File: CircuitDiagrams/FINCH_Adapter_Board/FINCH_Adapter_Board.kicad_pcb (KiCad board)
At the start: 2 copper layers, 195 x 101.7 mm, 59 parts, among them J1 CONN_02X20, J2 CONN_02X25, J3 CONN_02X10, J4 CONN_01X07, J5 CONN_01X10, SW1 DIPS_04, U1 7417, U10 74LS163, U11 74LS163, U12 74LS163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

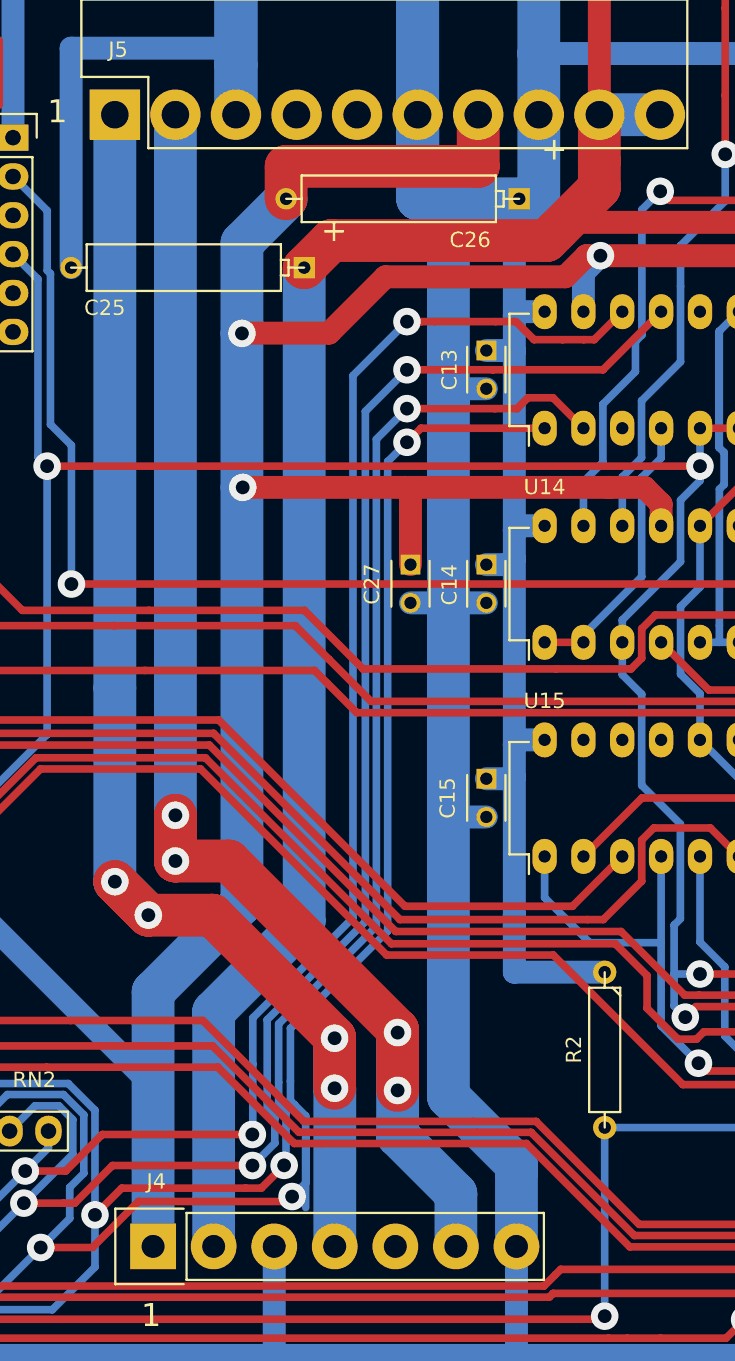
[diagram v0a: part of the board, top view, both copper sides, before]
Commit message: change 24V power supply a bit
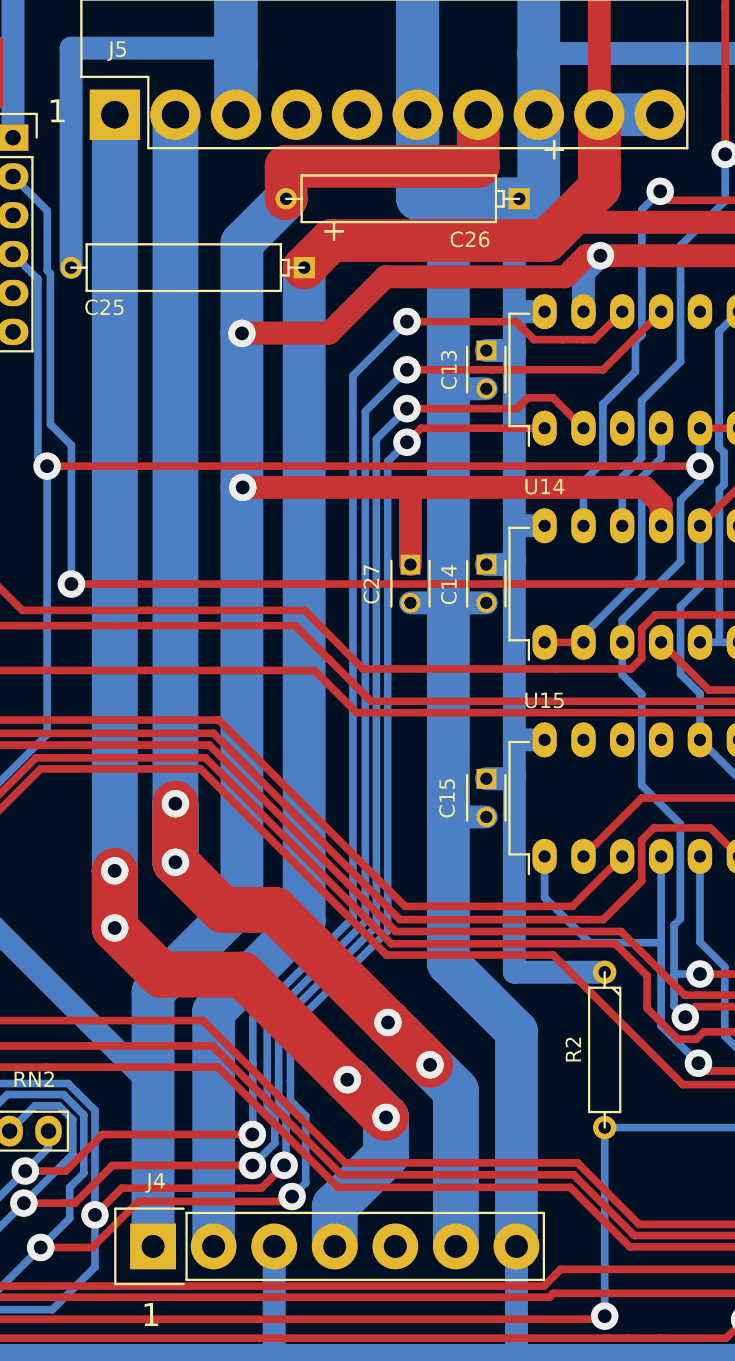
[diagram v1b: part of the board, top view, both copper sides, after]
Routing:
- net Net-(J4-Pad4): track 95.0 -> 100.7 mm
- net /FINCH_Adapter_Board_02/DRV_DATA_SERVO_READ_CLK_-: track 121.2 -> 116.6 mm
- net GND: track 1452.1 -> 1454.2 mm
- net Net-(J4-Pad6): track 93.6 -> 95.2 mm

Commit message: fix some stuff
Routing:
- net -5V: track 313.3 -> 300.3 mm
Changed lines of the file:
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@@
   (segment (start 53.57 135.7) (end 53.57 129.2) (width 1.5) (layer B.Cu) (net 2))
   (segment (start 146.44 135.7) (end 207.4 135.7) (width 1.5) (layer B.Cu) (net 2))
+  (segment (start 97.4 111.93) (end 91.22 111.93) (width 1.5) (layer B.Cu) (net 3))
+  (segment (start 91.22 111.93) (end 86.28 106.99) (width 1.5) (layer B.Cu) (net 3))
   (segment (start 85.61 106.99) (end 86.28 106.99) (width 1.5) (layer B.Cu) (net 3))
-  (segment (start 97.4 118.11) (end 97.4 128.57) (width 1.5) (layer B.Cu) (net 3))
-  (segment (start 86.28 106.99) (end 97.4 118.11) (width 1.5) (layer B.Cu) (net 3))
+  (segment (start 83.05 106.99) (end 85.61 106.99) (width 1.5) (layer B.Cu) (net 3))
   (segment (start 191.01 69.99) (end 195.78 69.99) (width 1.5) (layer F.Cu) (net 3))
   (segment (start 209.08 69.99) (end 210.64 69.99) (width 1.5) (layer F.Cu) (net 3))
@@
   (segment (start 71.62 108.09) (end 73.12 109.59) (width 1.5) (layer B.Cu) (net 3))
   (segment (start 82.47 107.57) (end 83.05 106.99) (width 1.5) (layer B.Cu) (net 3))
-  (segment (start 83.05 106.99) (end 85.61 106.99) (width 1.5) (layer B.Cu) (net 3))
   (segment (start 106.1 60.07) (end 103.21 62.96) (width 2.8) (layer B.Cu) (net 3))
   (segment (start 103.21 106.12) (end 97.4 111.93) (width 2.8) (layer B.Cu) (net 3))
